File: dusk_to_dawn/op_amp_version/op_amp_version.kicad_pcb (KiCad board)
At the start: 2 copper layers, 46 x 29 mm, 13 parts, among them J1 Conn_01x02_Pin, J2 Conn_01x02_Pin, J3 Conn_01x02_Pin, J4 Conn_01x02_Pin, U2 TLC372CP

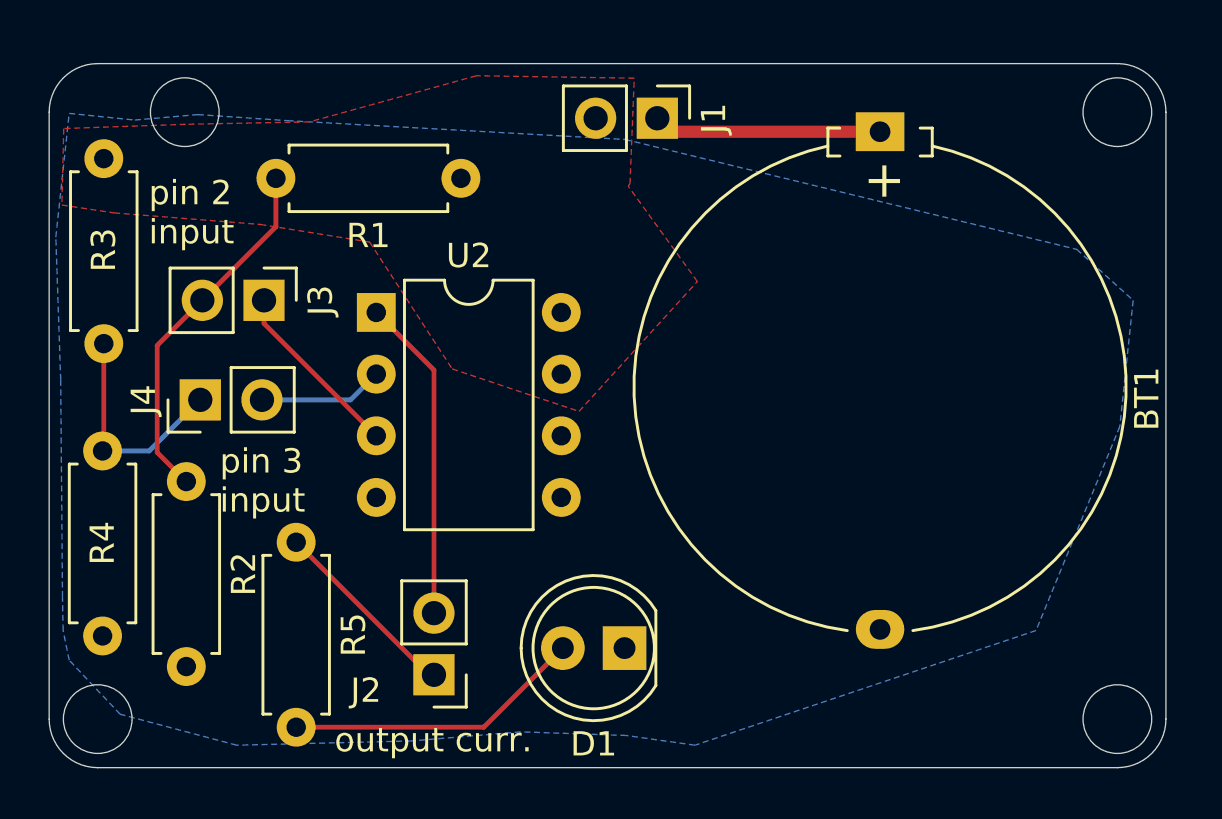
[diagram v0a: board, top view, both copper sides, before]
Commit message: add first version of op amp dusk to dawn
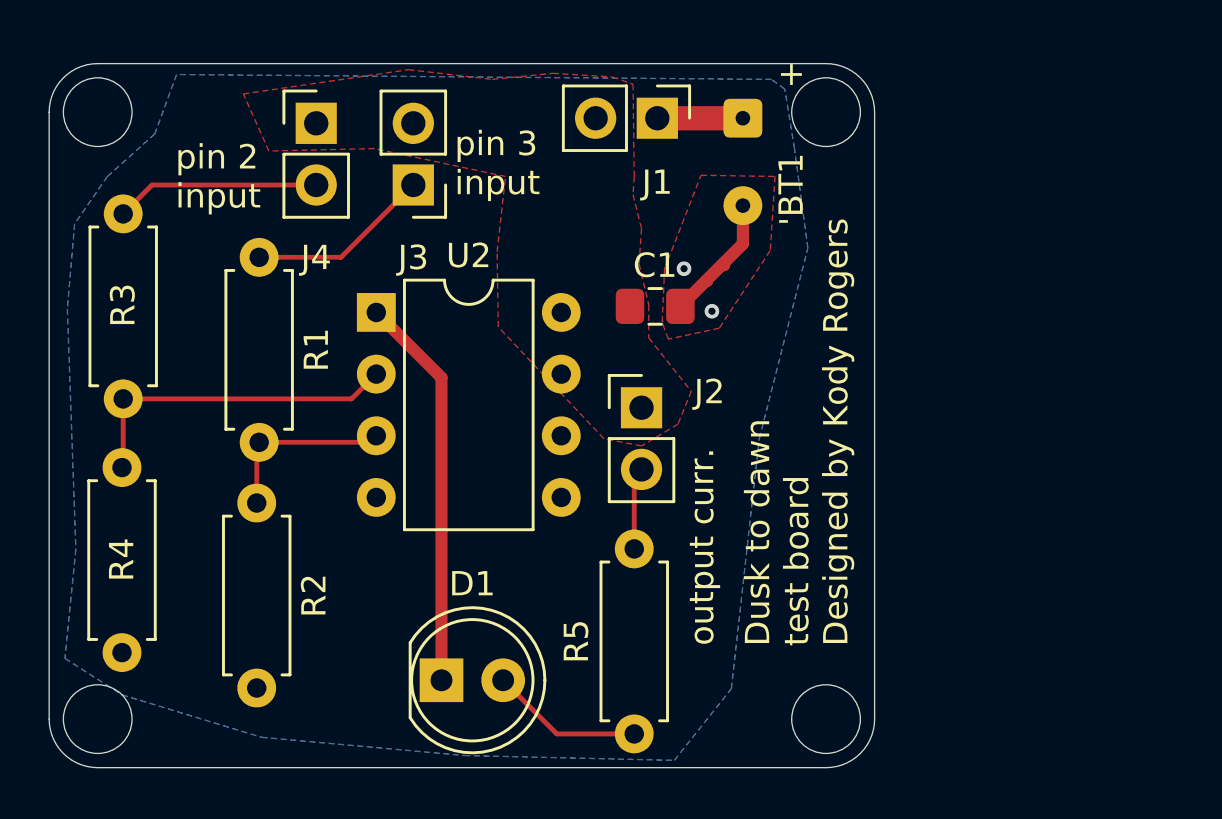
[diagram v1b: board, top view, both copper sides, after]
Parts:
- removed G***: LOGO, kicad_libraries:farm_hacks
- added C1: 0.01u, Capacitor_SMD:C_0805_2012Metric_Pad1.18x1.45mm_HandSolder, F.Cu at (170.0, 100.0)
- BT1: footprint Battery:Battery_Panasonic_CR2032-HFN_Horizontal_CircularHoles -> Connector_Wire:SolderWire-0.1sqmm_1x02_P3.6mm_D0.4mm_OD1mm
- R2: value 33k -> 330k
- R3: value 22k -> 33k
- R4: value 22k -> 330k
- moved R5 16.0 mm to (169.1, 117.6), turned to 90 degrees
- moved J2 13.9 mm to (169.4, 104.2), turned to 0 degrees
- moved J4 12.4 mm to (156.0, 92.5), turned to 0 degrees
- moved R1 8.92 mm to (153.7, 98.0), turned to -90 degrees
- moved J3 7.77 mm to (160.0, 95.0), turned to 180 degrees
- moved D1 7.66 mm to (161.2, 115.4), turned to 0 degrees
- moved BT1 5.68 mm to (173.6, 92.2)
- moved R2 3.03 mm to (153.6, 108.1)
- moved R3 2.41 mm to (148.1, 96.2)
- moved R4 1.05 mm to (148.0, 106.6)
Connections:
- net +3V0 renamed Net-(BT1-+)
- D1 pad 1: GND -> Net-(D1-K)
- J2 pad 1: Net-(J2-Pin_1) -> 3V
- J3 pad 2: Net-(J3-Pin_2) -> 3V
- J4 pad 1: Net-(J4-Pin_1) -> 3V
- R1 pad 1: 3V -> Net-(J3-Pin_1)
- R1 pad 2: Net-(J3-Pin_2) -> Net-(U2-+)
- R2 pad 1: Net-(J3-Pin_2) -> Net-(U2-+)
- R3 pad 1: 3V -> Net-(J4-Pin_2)
- R3 pad 2: Net-(J4-Pin_1) -> Net-(U2--)
- R4 pad 1: Net-(J4-Pin_1) -> Net-(U2--)
- R5 pad 1: Net-(J2-Pin_1) -> Net-(D1-A)
- R5 pad 2: Net-(D1-A) -> Net-(J2-Pin_2)
- U2 pad 1: Net-(J2-Pin_2) -> Net-(D1-K)
- U2 pad 2: Net-(J4-Pin_2) -> Net-(U2--)
- U2 pad 3: Net-(J3-Pin_1) -> Net-(U2-+)
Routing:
- net Net-(D1-K): track 0.00 -> 16.3 mm
- net Net-(J3-Pin_2): track 15.0 -> 0.00 mm
- net Net-(U2--): track 0.00 -> 13.7 mm
- net Net-(J2-Pin_2): track 13.4 -> 3.40 mm
- net Net-(J4-Pin_1): track 9.34 -> 0.00 mm
- net Net-(J2-Pin_1): track 7.94 -> 0.00 mm
- net Net-(U2-+): track 0.00 -> 7.48 mm
- net Net-(D1-A): track 12.3 -> 6.32 mm
- net Net-(BT1-+): track 9.41 -> 3.52 mm
- net GND: track 0.00 -> 5.30 mm, vias 0 -> 2
- net Net-(J4-Pin_2): track 5.15 -> 8.44 mm
- added copper zone on F.Cu, net GND
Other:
- board size 46 x 29 mm -> 34 x 29 mm
- board text added: "+"
- board text added: "-"
